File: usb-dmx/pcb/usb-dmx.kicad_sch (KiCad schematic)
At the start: 24 parts, among them J1 USB_C_Receptacle_USB2.0_16P, J2 USB_A, J3 Conn_01x01_Pin, J4 Conn_01x01_Socket, SW1 PTS526_SM15_SMTR2_LFS, U1 IP4234CZ6, U2 ADP2108AUJ-3.3, U3 ESP32-S3-MINI-1U, U4 ST485E

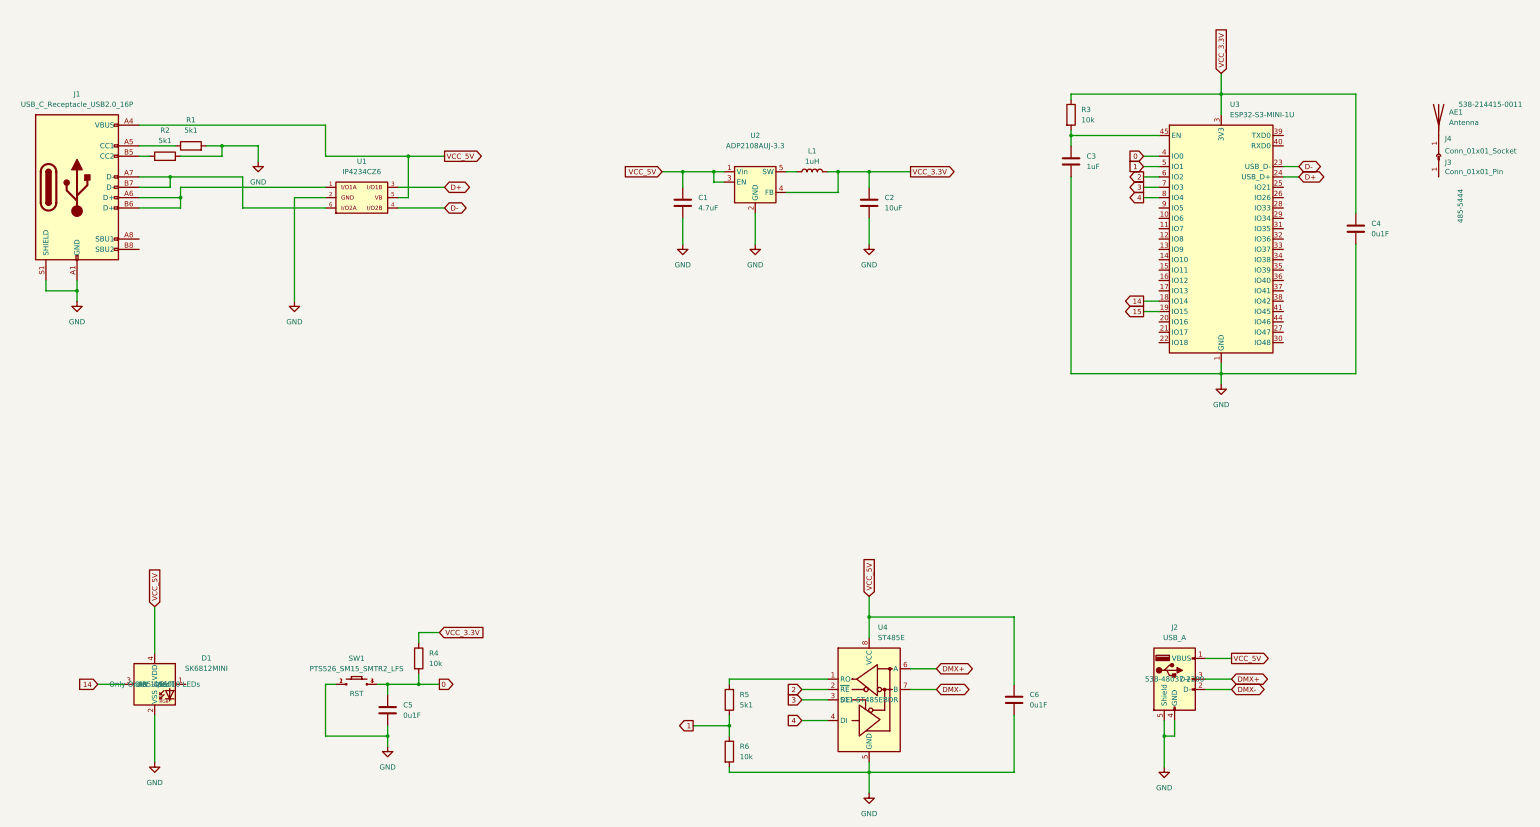
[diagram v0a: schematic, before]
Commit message: adding larger capacitor to esp and exchanging parts
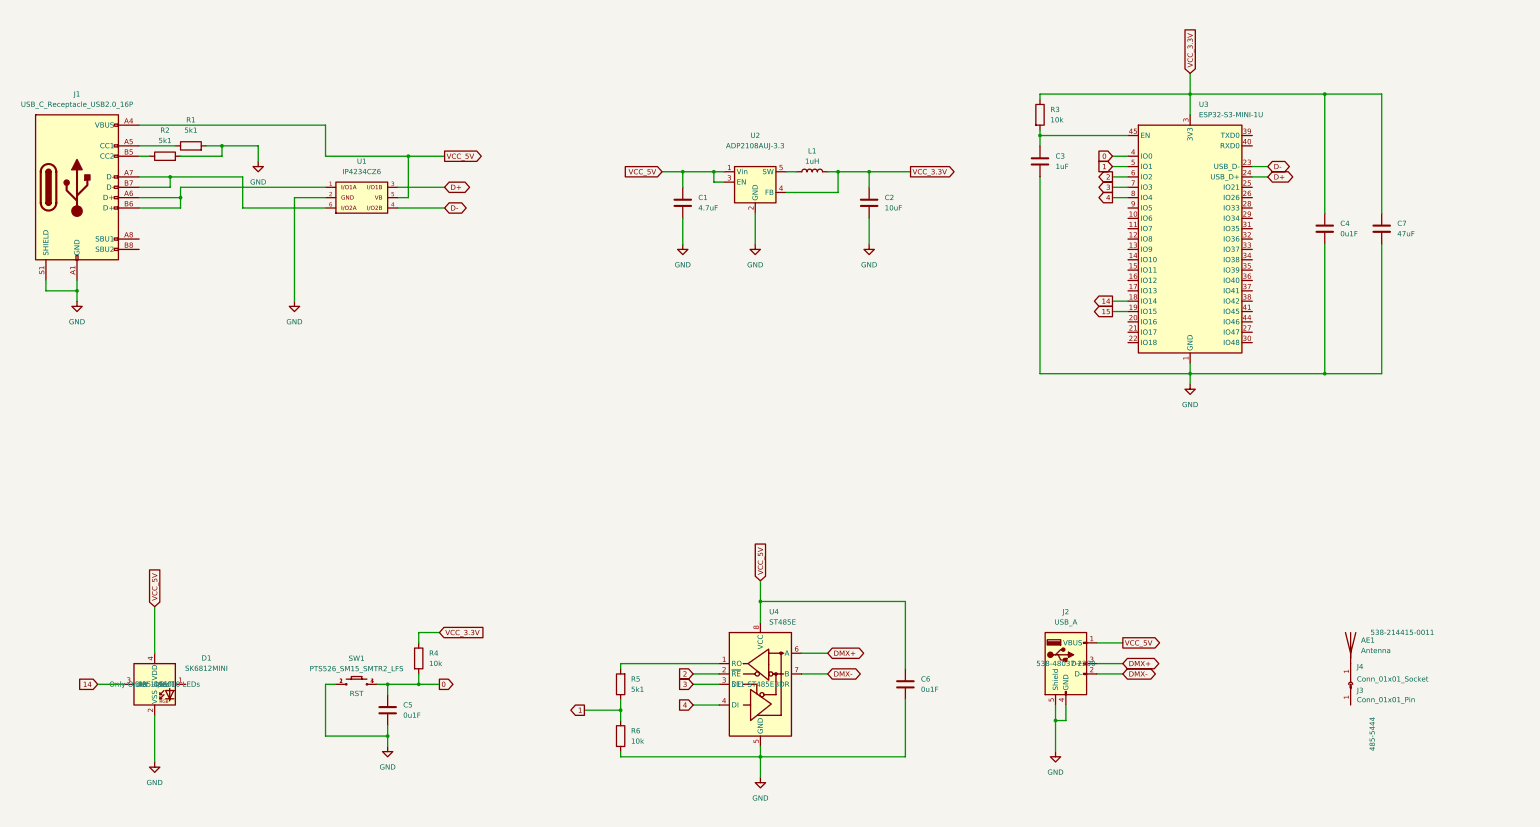
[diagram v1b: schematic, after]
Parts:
- added C7: 47uF, Capacitor_SMD:C_0805_2012Metric_Pad1.18x1.45mm_HandSolder, symbol Device:C
- J1: footprint Connector_USB:USB_C_Receptacle_GCT_USB4110 -> Connector_USB:USB_C_Receptacle_GCT_USB4105-xx-A_16P_TopMnt_Horizontal
- SW1: footprint footprints:PTS526SM15SMTR2LFS -> Button_Switch_SMD:SW_Push_1P1T_XKB_TS-1187A
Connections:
- net GND: now also C7.2
- net VCC_3.3V: now also C7.1
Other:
- moved on the sheet: AE1, C3, C4, C6, J2, J3, J4, R3, R5, R6, U3, U4

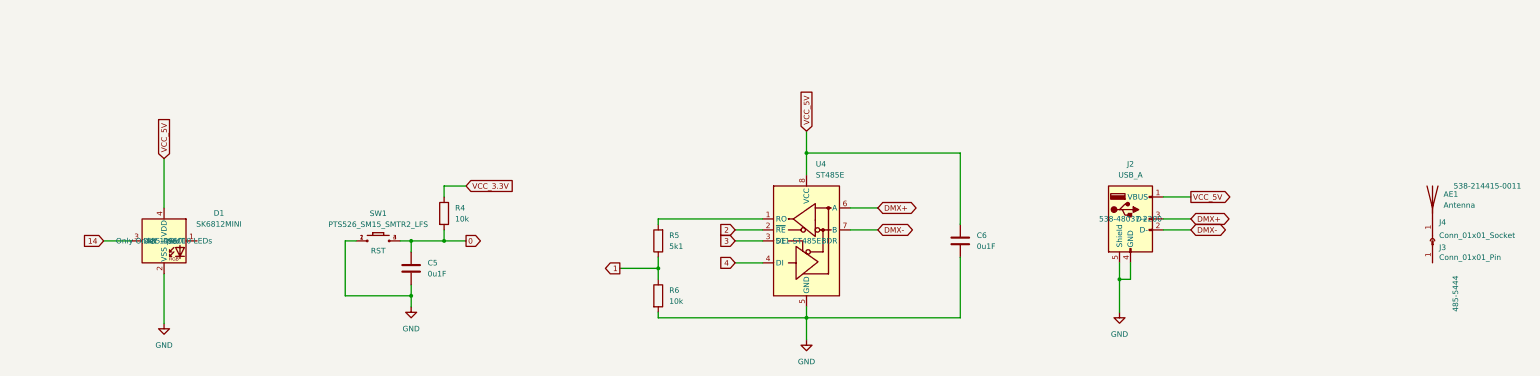
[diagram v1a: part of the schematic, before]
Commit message: fingind aliexpress alternatives
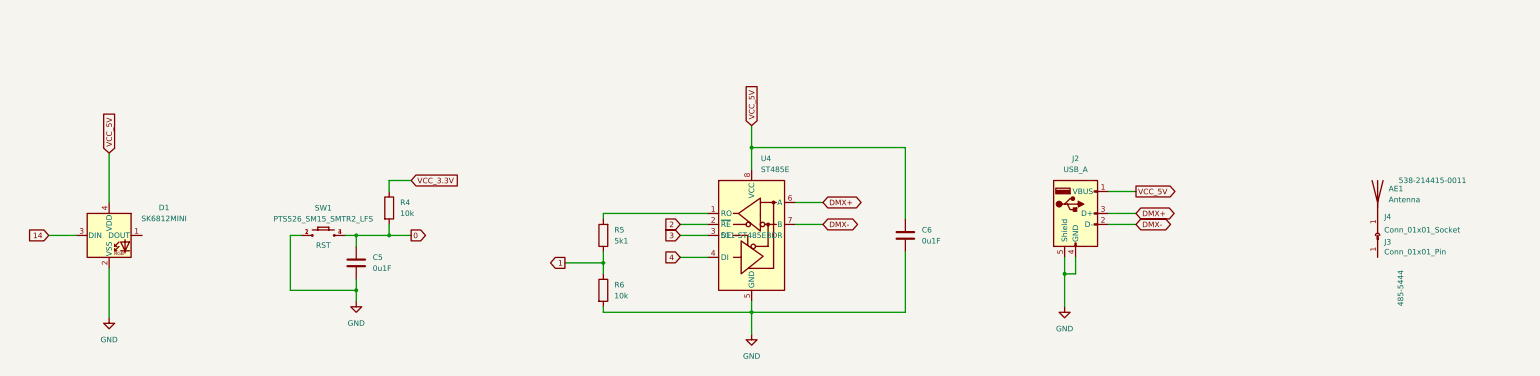
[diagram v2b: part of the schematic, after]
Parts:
- C1: ALIEXPRESS (none) -> https://de.aliexpress.com/item/1005006142309480.html; MOUSER_PART_NUMBER 187-CL10A475KP8NNWC -> (none)
- C2: ALIEXPRESS (none) -> https://de.aliexpress.com/item/1005006142309480.html; MOUSER_PART_NUMBER 187-CL21A106KOQNNNF -> (none)
- C3: ALIEXPRESS (none) -> https://de.aliexpress.com/item/1005003512666695.html; MOUSER_PART_NUMBER 187-CL10B105KA8NNND -> (none)
- C4, C5, C6: ALIEXPRESS (none) -> https://de.aliexpress.com/item/1005003512666695.html; MOUSER_PART_NUMBER 187-CL10B104KA8NNNC -> (none)
- C7: ALIEXPRESS (none) -> https://de.aliexpress.com/item/1005006142309480.html; MOUSER_PART_NUMBER 187-CL10B104KA8NNNC -> (none)
- D1: ALIEXPRESS (none) -> https://de.aliexpress.com/item/33015141472.html; DESCRIPTION Only Order 1 per 10 LEDs -> (none); MOUSER_PART_NUMBER 485-4960 -> (none)
- J1: ALIEXPRESS (none) -> https://de.aliexpress.com/item/1005008805157100.html; MOUSER_PART_NUMBER 640-USB4110-GF-A -> (none)
- J2: footprint Connector_USB:USB_A_Molex_48037-2200_Horizontal -> Connector_USB:USB_A_CNCTech_1001-011-01101_Horizontal; ALIEXPRESS (none) -> https://de.aliexpress.com/item/4000649452665.html; MOUSER_PART_NUMBER 538-48037-2200 -> (none)
- R1, R2, R5: ALIEXPRESS (none) -> https://de.aliexpress.com/item/1005002384017954.html; MOUSER_PART_NUMBER 71-CRCW0603-5.1K-E3 -> (none)
- R3, R4, R6: ALIEXPRESS (none) -> https://de.aliexpress.com/item/1005002384017954.html; MOUSER_PART_NUMBER 71-CRCW0603-10K-E3 -> (none)
- SW1: ALIEXPRESS (none) -> https://de.aliexpress.com/item/1005006151795450.html; MOUSER_PART_NUMBER 611-PTS526SM15SMTR2L -> (none)
- U3: ALIEXPRESS (none) -> https://de.aliexpress.com/item/1005005230617287.html; MOUSER_PART_NUMBER 356-ESP32S3MINI1UN8 -> (none)
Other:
- moved on the sheet: AE1, C5, C6, D1, J2, J3, J4, R4, R5, R6, SW1, U4

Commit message: creating pcb layout
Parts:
- removed L1: 1uH, Inductor_SMD:L_0805_2012Metric, symbol Device:L
- removed SW1: PTS526_SM15_SMTR2_LFS, Button_Switch_SMD:SW_Push_1P1T_XKB_TS-1187A, symbol PTS526_SM15_SMTR2_LFS:PTS526_SM15_SMTR2_LFS
- removed U1: IP4234CZ6, footprints:IP4234CZ6_SOT-457-6, symbol IP4234CZ6:IP4234CZ6
- removed U2: ADP2108AUJ-3.3, Package_TO_SOT_SMD:TSOT-23-5, symbol Regulator_Switching:ADP2108AUJ-3.3
- removed U4: ST485E, Package_SO:SOIC-8_3.9x4.9mm_P1.27mm, symbol Interface_UART:ST485E
- added SW2: SW_Push, Button_Switch_SMD:SW_Push_1P1T_XKB_TS-1187A, symbol Switch:SW_Push
- added U1: AMS1117-3.3, Package_TO_SOT_SMD:SOT-223-3_TabPin2, symbol Regulator_Linear:AMS1117-3.3
- added U4: USBLC6-2SC6, Package_TO_SOT_SMD:SOT-23-6, symbol Power_Protection:USBLC6-2SC6
- added U5: MAX485E, Package_SO:SOP-8_3.76x4.96mm_P1.27mm, symbol Interface_UART:MAX485E
- C1: value 4.7uF -> 22uF; footprint Capacitor_SMD:C_0603_1608Metric -> Capacitor_SMD:C_0805_2012Metric
- C2: value 10uF -> 22uF
- C5: footprint Capacitor_SMD:C_0603_1608Metric_Pad1.08x0.95mm_HandSolder -> Capacitor_SMD:C_0603_1608Metric
- R4: footprint Resistor_SMD:R_0603_1608Metric_Pad0.98x0.95mm_HandSolder -> Resistor_SMD:R_0603_1608Metric
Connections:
- net 0: now also SW2.2
- net 2: now also U5.2 (~{RE})
- net 3: now also U5.3 (DE)
- net 4: now also U5.4 (DI)
- net D+: now also U4.6 (I/O1)
- net D-: now also U4.4 (I/O2)
- net DMX+: now also U5.6 (A)
- net DMX-: now also U5.7 (B)
- net GND: now also SW2.1, U1.1 (GND), U4.2 (GND), U5.5 (GND)
- net VCC_3.3V: now also C1.1, U1.2 (VO); no longer C2.1
- net VCC_5V: now also C2.1, U1.3 (VI), U4.5 (VBUS), U5.8 (VCC); no longer C1.1
- net at R5.2: now also U5.1 (RO)
- net at J1.A6 (D+), J1.B6 (D+): now also U4.1 (I/O1)
- net at J1.A7 (D-), J1.B7 (D-): now also U4.3 (I/O2)
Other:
- moved on the sheet: C3, C4, C7, R3, U3

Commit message: updating documentation
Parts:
- removed AE1: Antenna, symbol Device:Antenna
- removed J3: Conn_01x01_Pin, symbol Connector:Conn_01x01_Pin
- removed J4: Conn_01x01_Socket, symbol Connector:Conn_01x01_Socket
- J1: value USB_C_Receptacle_USB2.0_16P -> USB_C_Receptacle
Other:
- company: Author: Samuel Hafen -> Hafen Innovation
- title: USB-DMX -> TRANCE USB-DMX
- moved on the sheet: C1, C2, J2, U1

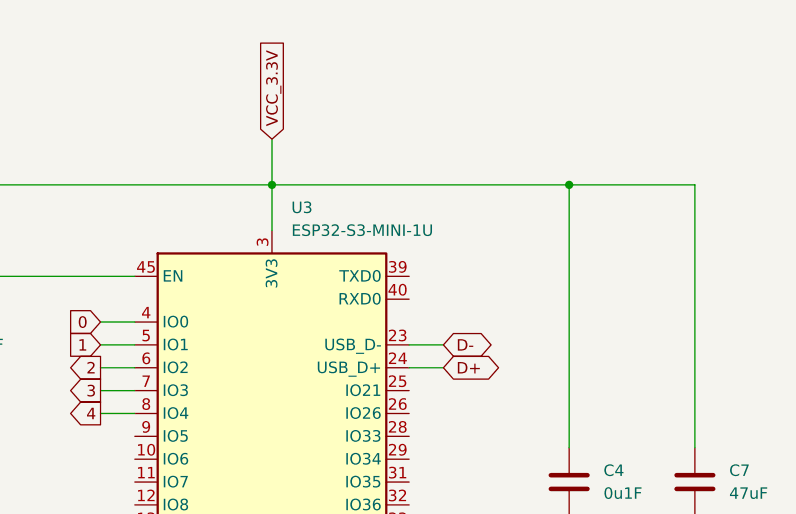
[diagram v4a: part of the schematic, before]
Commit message: moving usb-a-plug, changing esp32-partnumber
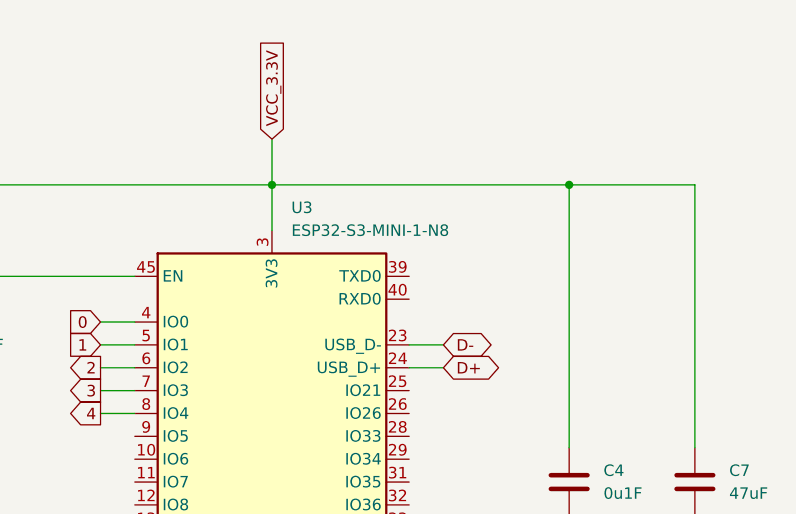
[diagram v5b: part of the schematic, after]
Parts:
- U3: value ESP32-S3-MINI-1U -> ESP32-S3-MINI-1-N8
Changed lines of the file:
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@@
 			)
 		)
-		(property "Value" "ESP32-S3-MINI-1U"
+		(property "Value" "ESP32-S3-MINI-1-N8"
 			(at 323.4533 53.34 0)
 			(effects
